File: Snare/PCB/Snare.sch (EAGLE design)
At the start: 91 parts, among them IC1 LM741P, IC10 LM741P, IC6 LM741P, IC7 LM741P, IC8 LM741P, IC9 LM741P, Q3 2N2222A, Q4 2N2222A, T1 2N3904, T5 2N3904, T6 2N3904

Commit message: Updated Snare schematic
updated snare schematic
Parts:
- added R11: 4.7k, resistor:R-US_0207/10
- added R12: 10k, rcl:R-TRIMM64W
- R1: value 10k -> 2k
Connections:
- removed net VCA_OUT: IC10.OUT, R60.1, R9.2
- new net DRUM_OUTPUT: C47.1, IC9.OUT, R12.E, R55.1, R56.2
- net AGND: now also R11.2, R12.A
- net N$27: now also R11.1
- net POT1A: now also R12.S; no longer C47.1, IC9.OUT, R55.1, R56.2
- net SW1: now also IC10.OUT, R60.1
- net SW2: now also R9.2
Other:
- note added: "Note: 1) POT1A is the drum output 2) The third pin of POT1 should be grounded 3) POT1B should be the middle pin of the POT"
- note added: "Note: 1) Switch turns the snare on/off 2) SW1 and SW2 normally connected 3) SW3 should be left open on the pot board"
- note removed: "Note: The third pin of POT1 should be grounded POT1B should be the middle pin"
- moved on the sheet: C38, R44

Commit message: Started PCB
Started working on the PCB
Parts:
- R100: value 2k -> 47k
- R101: value 2k -> 100k
- renumbered 100K to R101, 47K to R100
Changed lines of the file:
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@@
 <part name="IC6" library="linear" library_urn="urn:adsk.eagle:library:262" deviceset="*741" device="P" package3d_urn="urn:adsk.eagle:package:16409/2" technology="LM"/>
 <part name="C35" library="resistor" library_urn="urn:adsk.eagle:library:348" deviceset="C-EU" device="050-024X044" package3d_urn="urn:adsk.eagle:package:26162/1" value="0.1uF"/>
-<part name="100K" library="resistor" library_urn="urn:adsk.eagle:library:348" deviceset="R-US_" device="0207/10" package3d_urn="urn:adsk.eagle:package:25939/1" value="2k"/>
+<part name="R101" library="resistor" library_urn="urn:adsk.eagle:library:348" deviceset="R-US_" device="0207/10" package3d_urn="urn:adsk.eagle:package:25939/1" value="100k"/>
 <part name="C36" library="resistor" library_urn="urn:adsk.eagle:library:348" deviceset="C-EU" device="050-024X044" package3d_urn="urn:adsk.eagle:package:26162/1" value="0.1uF"/>
 <part name="C37" library="resistor" library_urn="urn:adsk.eagle:library:348" deviceset="C-EU" device="050-024X044" package3d_urn="urn:adsk.eagle:package:26162/1" value="0.1uF"/>
-<part name="47K" library="resistor" library_urn="urn:adsk.eagle:library:348" deviceset="R-US_" device="0207/10" package3d_urn="urn:adsk.eagle:package:25939/1" value="2k"/>
+<part name="R100" library="resistor" library_urn="urn:adsk.eagle:library:348" deviceset="R-US_" device="0207/10" package3d_urn="urn:adsk.eagle:package:25939/1" value="47k"/>
 <part name="IC7" library="linear" library_urn="urn:adsk.eagle:library:262" deviceset="*741" device="P" package3d_urn="urn:adsk.eagle:package:16409/2" technology="LM"/>
 <part name="C38" library="resistor" library_urn="urn:adsk.eagle:library:348" deviceset="C-EU" device="050-024X044" package3d_urn="urn:adsk.eagle:package:26162/1" value="1nF"/>
@@
 <attribute name="VALUE" x="38.481" y="257.556" size="1.778" layer="96" rot="R270"/>
 </instance>
-<instance part="100K" gate="G$1" x="88.9" y="287.02" smashed="yes" rot="R180">
+<instance part="R101" gate="G$1" x="88.9" y="287.02" smashed="yes" rot="R180">
 <attribute name="NAME" x="90.17" y="285.5214" size="1.778" layer="95" rot="R180"/>
 <attribute name="VALUE" x="92.71" y="290.322" size="1.778" layer="96" rot="R180"/>
@@
 <attribute name="VALUE" x="86.741" y="275.336" size="1.778" layer="96" rot="R270"/>
 </instance>
-<instance part="47K" gate="G$1" x="55.88" y="259.08" smashed="yes" rot="R180">
+<instance part="R100" gate="G$1" x="55.88" y="259.08" smashed="yes" rot="R180">
 <attribute name="NAME" x="57.15" y="257.5814" size="1.778" layer="95" rot="R180"/>
 <attribute name="VALUE" x="59.69" y="262.382" size="1.778" layer="96" rot="R180"/>
@@
 <pinref part="IC6" gate="A" pin="-IN"/>
 <wire x1="76.2" y1="259.08" x2="71.12" y2="259.08" width="0.1524" layer="91"/>
-<pinref part="100K" gate="G$1" pin="2"/>
+<pinref part="R101" gate="G$1" pin="2"/>
 <wire x1="71.12" y1="259.08" x2="71.12" y2="287.02" width="0.1524" layer="91"/>
 <wire x1="71.12" y1="287.02" x2="83.82" y2="287.02" width="0.1524" layer="91"/>
-<pinref part="47K" gate="G$1" pin="1"/>
+<pinref part="R100" gate="G$1" pin="1"/>
 <wire x1="71.12" y1="259.08" x2="60.96" y2="259.08" width="0.1524" layer="91"/>
 <junction x="71.12" y="259.08"/>
@@
 <net name="WHITE_NOISE_AMP" class="0">
 <segment>
-<pinref part="100K" gate="G$1" pin="1"/>
+<pinref part="R101" gate="G$1" pin="1"/>
 <wire x1="93.98" y1="287.02" x2="116.84" y2="287.02" width="0.1524" layer="91"/>
 <wire x1="116.84" y1="287.02" x2="116.84" y2="261.62" width="0.1524" layer="91"/>
@@
 <net name="N$28" class="0">
 <segment>
-<pinref part="47K" gate="G$1" pin="2"/>
+<pinref part="R100" gate="G$1" pin="2"/>
 <pinref part="C35" gate="G$1" pin="1"/>
 <wire x1="50.8" y1="259.08" x2="45.72" y2="259.08" width="0.1524" layer="91"/>

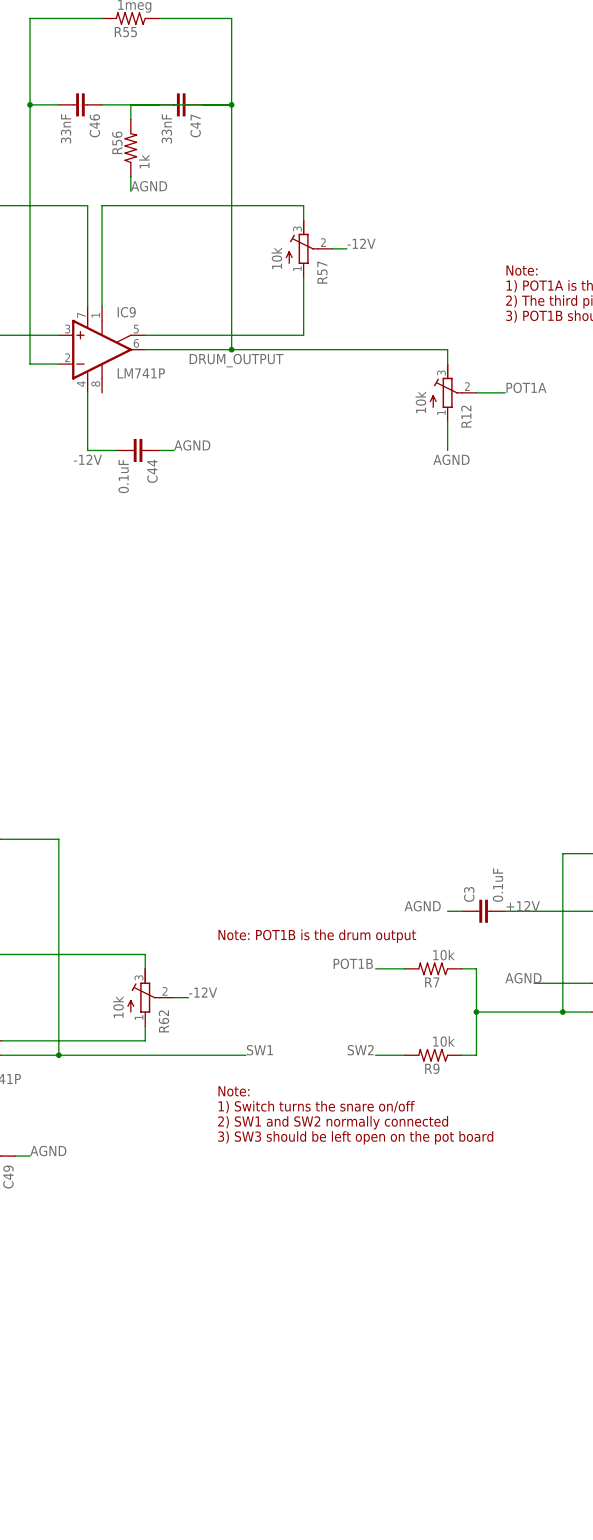
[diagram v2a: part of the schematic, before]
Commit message: Finished PCB
Finished the snare PCB
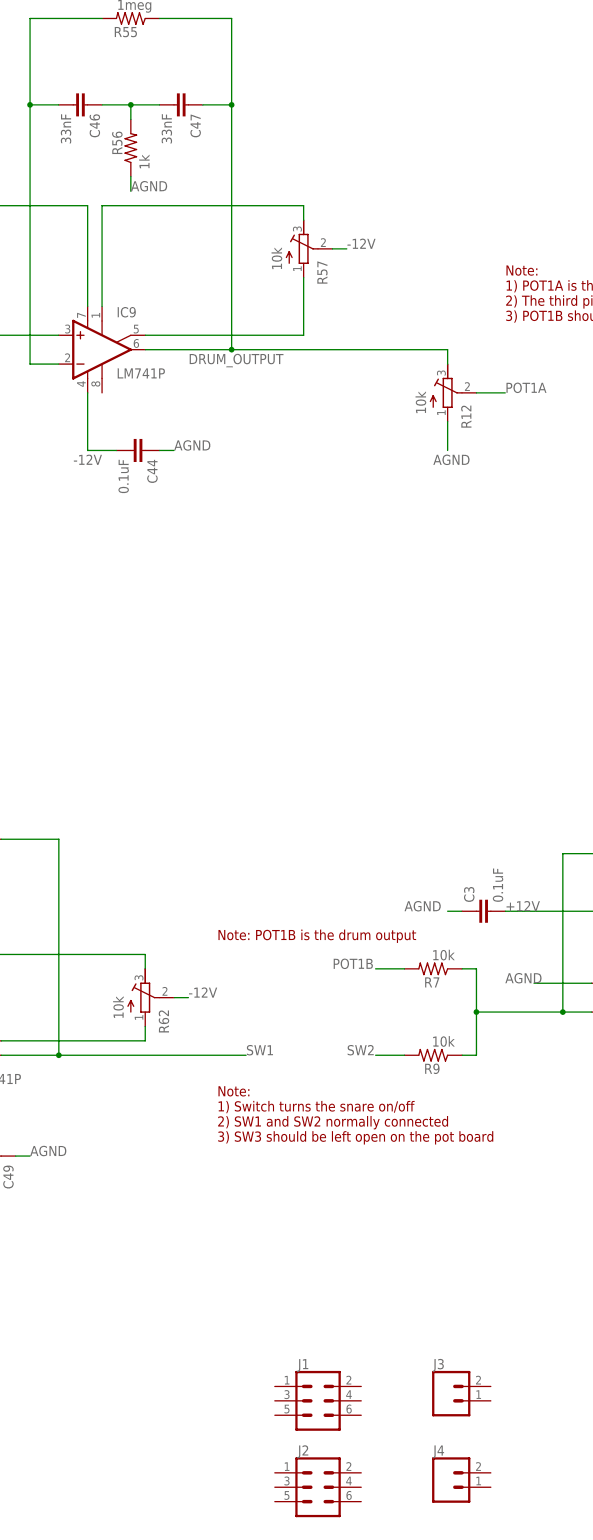
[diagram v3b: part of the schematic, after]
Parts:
- added J1, J2: (no value), SparkFun-Connectors:CONN_03X2NO_SILK
- added J3, J4: (no value), SparkFun-Connectors:CONN_021X02_NO_SILK
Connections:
- removed net N$44: C46.1, C47.2
- new net N$8: C46.1, C47.2, R56.2
- net DRUM_OUTPUT: no longer R56.2
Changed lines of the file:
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@@
 <part name="R11" library="resistor" library_urn="urn:adsk.eagle:library:348" deviceset="R-US_" device="0207/10" package3d_urn="urn:adsk.eagle:package:25939/1" value="4.7k"/>
 <part name="R12" library="rcl" library_urn="urn:adsk.eagle:library:334" deviceset="R-TRIMM" device="64W" package3d_urn="urn:adsk.eagle:package:23748/1" value="10k"/>
+<part name="J1" library="SparkFun-Connectors" deviceset="CONN_03X2" device="NO_SILK"/>
+<part name="J2" library="SparkFun-Connectors" deviceset="CONN_03X2" device="NO_SILK"/>
+<part name="J3" library="SparkFun-Connectors" deviceset="CONN_02" device="1X02_NO_SILK"/>
+<part name="J4" library="SparkFun-Connectors" deviceset="CONN_02" device="1X02_NO_SILK"/>
 </parts>
 <sheets>
@@
 <attribute name="NAME" x="377.571" y="250.19" size="1.778" layer="95" rot="R90"/>
 <attribute name="VALUE" x="369.57" y="252.73" size="1.778" layer="96" rot="R90"/>
+</instance>
+<instance part="J1" gate="G$1" x="350.52" y="78.74" smashed="yes">
+<attribute name="NAME" x="346.964" y="84.328" size="1.778" layer="95" font="vector"/>
+<attribute name="VALUE" x="347.218" y="72.898" size="1.778" layer="96" font="vector" align="top-left"/>
+</instance>
+<instance part="J2" gate="G$1" x="350.52" y="63.5" smashed="yes">
+<attribute name="NAME" x="346.964" y="69.088" size="1.778" layer="95" font="vector"/>
+<attribute name="VALUE" x="347.218" y="57.658" size="1.778" layer="96" font="vector" align="top-left"/>
+</instance>
+<instance part="J3" gate="G$1" x="373.38" y="78.74" smashed="yes">
+<attribute name="VALUE" x="370.84" y="73.914" size="1.778" layer="96" font="vector"/>
+<attribute name="NAME" x="370.84" y="84.328" size="1.778" layer="95" font="vector"/>
+</instance>
+<instance part="J4" gate="G$1" x="373.38" y="63.5" smashed="yes">
+<attribute name="VALUE" x="370.84" y="58.674" size="1.778" layer="96" font="vector"/>
+<attribute name="NAME" x="370.84" y="69.088" size="1.778" layer="95" font="vector"/>
 </instance>
 </instances>
@@
 </segment>
 </net>
-<net name="N$44" class="0">
-<segment>
-<pinref part="C46" gate="G$1" pin="1"/>
-<pinref part="C47" gate="G$1" pin="2"/>
-<wire x1="312.42" y1="307.34" x2="322.58" y2="307.34" width="0.1524" layer="91"/>
-</segment>
-</net>
 <net name="N$48" class="0">
 <segment>
@@
 <pinref part="R55" gate="G$1" pin="1"/>
 <wire x1="322.58" y1="322.58" x2="335.28" y2="322.58" width="0.1524" layer="91"/>
+<pinref part="IC9" gate="A" pin="OUT"/>
 <wire x1="335.28" y1="322.58" x2="335.28" y2="307.34" width="0.1524" layer="91"/>
-<pinref part="IC9" gate="A" pin="OUT"/>
 <wire x1="335.28" y1="307.34" x2="335.28" y2="264.16" width="0.1524" layer="91"/>
 <wire x1="335.28" y1="264.16" x2="320.04" y2="264.16" width="0.1524" layer="91"/>
 <label x="327.66" y="261.62" size="1.778" layer="95"/>
-<pinref part="C47" gate="G$1" pin="1"/>
-<wire x1="330.2" y1="307.34" x2="335.28" y2="307.34" width="0.1524" layer="91"/>
-<junction x="335.28" y="307.34"/>
-<pinref part="R56" gate="G$1" pin="2"/>
-<wire x1="335.28" y1="307.34" x2="317.5" y2="307.34" width="0.1524" layer="91"/>
-<wire x1="317.5" y1="307.34" x2="317.5" y2="304.8" width="0.1524" layer="91"/>
 <wire x1="335.28" y1="264.16" x2="373.38" y2="264.16" width="0.1524" layer="91"/>
 <junction x="335.28" y="264.16"/>
 <pinref part="R12" gate="G$1" pin="E"/>
 <wire x1="373.38" y1="261.62" x2="373.38" y2="264.16" width="0.1524" layer="91"/>
-</segment>
-</net>
+<pinref part="C47" gate="G$1" pin="1"/>
+<wire x1="330.2" y1="307.34" x2="335.28" y2="307.34" width="0.1524" layer="91"/>
+<junction x="335.28" y="307.34"/>
+</segment>
+</net>
+<net name="N$8" class="0">
+<segment>
+<pinref part="R56" gate="G$1" pin="2"/>
+<wire x1="317.5" y1="307.34" x2="317.5" y2="304.8" width="0.1524" layer="91"/>
+<pinref part="C46" gate="G$1" pin="1"/>
+<wire x1="312.42" y1="307.34" x2="317.5" y2="307.34" width="0.1524" layer="91"/>
+<pinref part="C47" gate="G$1" pin="2"/>
+<wire x1="317.5" y1="307.34" x2="322.58" y2="307.34" width="0.1524" layer="91"/>
+<junction x="317.5" y="307.34"/>
+</segment>
+</net>

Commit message: Finished Silkscreen
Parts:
- removed C38: 1nF, resistor:C-EU050-024X044
- removed C41: 2.2u, resistor:C-EU050-024X044
- removed C42: 10uF, rcl:CPOL-USE2.5-6
- removed C43, C44, C45, C49, C50: 0.1uF, resistor:C-EU050-024X044
- removed C47: 33nF, resistor:C-EU050-024X044
- removed D6: 200mA/100V/1V, SparkFun-DiscreteSemi:DIODE-1N4148
- removed R100, R51: 47k, resistor:R-US_0207/10
- removed R101: 100k, resistor:R-US_0207/10
- removed R34: 680k, resistor:R-US_0207/10
- removed R39, R40: 2k, resistor:R-US_0207/10
- removed R46: 15k, resistor:R-US_0207/10
- removed R49: 10k, resistor:R-US_0207/10
- removed R50: 220, resistor:R-US_0207/10
- added C10, C6, C9: 0.1uF, resistor:C-EU050-024X044
- added C13, C14, C16: 10uF, rcl:CPOL-USE2.5-6
- added C17, C18: 1u, resistor:C-EU050-024X044
- added C4: 1nF, resistor:C-EU050-024X044
- added D2: 200mA/100V/1V, SparkFun-DiscreteSemi:DIODE-1N4148
- added R13: 1k, resistor:R-US_0207/10
- added R14, R16: 100k, resistor:R-US_0207/10
- added R15, R17, R18: 10k, resistor:R-US_0207/10
- added TRIM3, TRIM4, TRIM6: 10k, rcl:R-TRIMM64W
- C15: value 0.33uF -> 10uF; device resistor:C-EU050-024X044 -> rcl:CPOL-USE2.5-6
- C2: value 0.1uF -> 1nF
- C20: value 1nF -> 0.33uF
- C23: value 2.2u -> 0.1uF
- C24, C28: value 10uF -> 0.1uF; device rcl:CPOL-USE2.5-6 -> resistor:C-EU050-024X044
- C26, C29: value 1u -> 0.1uF
- C27: value 1u -> 33nF
- C3: value 0.1uF -> 10uF; device resistor:C-EU050-024X044 -> rcl:CPOL-USE2.5-6
- C30: value 0.1uF -> 2.2u
- C31: value 10uF -> 1u; device rcl:CPOL-USE2.5-6 -> resistor:C-EU050-024X044
- C32: value 10uF -> 2.2u; device rcl:CPOL-USE2.5-6 -> resistor:C-EU050-024X044
- R1: value 2k -> 15k
- R10: device rcl:R-TRIMM64W -> resistor:R-US_0207/10
- R11: value 4.7k -> 2k
- R12: value 10k -> 4.7k; device rcl:R-TRIMM64W -> resistor:R-US_0207/10
- R2: value 100k -> 47k
- R3, R4: value 10k -> 2k
- R35: value 1k -> 10k
- R36: value 100k -> 10k
- R38: value 4.7k -> 1k
- R43: value 2k -> 220
- R44: value 15k -> 10k
- R45: value 10k -> 47k
- R5: value 10k -> 15k
- R6: value 1k -> 2k
- R7: value 10k -> 4.7k
- R8: value 10k -> 680k; device rcl:R-TRIMM64W -> resistor:R-US_0207/10
- R9: value 10k -> 100k
- renumbered C34 to C5, C35 to C1, C36 to C8, C37 to C7, C39 to C12, C40 to C11, C46 to C25, C48 to C19, IC10 to IC4, IC7 to IC3, IC8 to IC2, IC9 to IC5, R47 to R41, R48 to R42, R52 to R20, R53 to R27, R54 to R29, R55 to R31, R56 to R32, R57 to TRIM5, R58 to R21, R59 to R28, R60 to R30, R61 to R22, R62 to TRIM2, R63 to TRIM1, R64 to R23, R65 to R19, R66 to R25, R67 to R26, T1 to Q1, T5 to Q2, T6 to Q6, U$1 to Q5
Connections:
- net +12V: now also C15.+, C17.2, C21.2, C23.1, C28.2, C9.2, R3.1, R43.2; no longer C22.2, C24.+, C27.2, C3.2, C45.1, C50.2, R39.1, R50.2
- net -12V: now also C10.2, C16.-, C18.1, C24.2, C26.2, C29.2, R4.2, R44.1, TRIM4.S; no longer C2.2, C21.2, C28.-, C29.1, C44.2, C49.2, R10.S, R40.2, R49.1
- net AGND: now also C10.1, C15.-, C16.+, C17.1, C18.2, C20.1, C23.2, C24.1, C26.1, C28.1, C29.1, C31.2, C33.-, C4.2, C9.1, R14.2, R45.1, R5.2, R6.2, R7.2, TRIM6.A; no longer C15.1, C2.1, C20.2, C22.1, C24.-, C26.2, C27.1, C28.+, C29.2, C3.1, C42.-, C44.1, C45.2, C49.1, C50.1, R1.2, R11.2, R12.A, R2.2, R44.2, R51.1
- net CC_INPUT: now also C30.2, IC6.OUT, TRIM3.S; no longer C23.2, IC1.OUT, R8.S
- net DRUM_OUTPUT: now also C27.1, TRIM6.E; no longer C47.1, R12.E
- net LOW_FREQ_WN: now also R10.1, R15.2; no longer R3.2, R45.1
- net N$1: now also R15.1, R17.1, R18.2; no longer R3.1, R4.2, R5.1
- net N$2: now also IC6.-IN, R35.1, R36.1, R38.2; no longer IC1.-IN, R6.2, R7.1, R9.1
- net N$20: now also C6.1, R8.2; no longer C30.1, R34.2
- net N$21: now also C14.-, C3.-, R13.2, R16.2, R4.1; no longer C31.-, C33.-, R35.2, R36.2, R40.1
- net N$23: now also IC1.-IN, R2.1, R9.2; no longer IC6.-IN, R100.1, R101.2
- net N$27: now also R11.2, R7.1; no longer R11.1, R43.2
- net N$28: now also R2.2; no longer R100.2
- net N$3: now also R38.1, TRIM3.A; no longer R6.1, R8.A
- net N$30: now also C13.+, R12.2; no longer C32.+, R38.2
- net N$32: now also C2.1, R5.1; no longer C38.1, R44.1
- net N$33: now also R10.2, R6.1; no longer R1.1, R45.2
- net N$34: now also C4.1, R1.2; no longer C20.1, R46.2
- net N$36: now also C20.2, C22.2, D2.C; no longer C15.2, C43.2, D1.C
- net N$37: now also C30.1; no longer C23.1
- net N$38: now also C32.1, R44.2; no longer C41.1, R49.2
- net N$39: now also C31.1, C33.+, R43.1; no longer C26.1, C42.+, R50.1
- net N$4: now also IC6.ON2, TRIM4.A; no longer IC1.ON2, R10.A
- net N$40: now also D2.A, Q4.E; no longer D1.A, Q3.E
- net N$41: now also C22.1; no longer C43.1
- net N$5: now also C14.+, R13.1; no longer C31.+, R35.1
- net N$51: now also D1.C; no longer D6.C
- net N$53: now also D1.A, Q3.E; no longer D6.A, Q4.E
- net N$6: now also C3.+, C6.2, R12.1, R3.2, R8.1; no longer C30.2, C33.+, R34.1, R38.1, R39.2
- net N$7: now also IC6.ON1, TRIM4.E; no longer IC1.ON1, R10.E
- net N$8: now also C27.2; no longer C47.2
- net OUTPUT: now also C32.2, R45.2; no longer C41.2, R51.2
- net POT1A: now also TRIM6.S; no longer R12.S
- net POT1B: now also R35.2; no longer R7.2
- net POT2A: now also R11.1; no longer R43.1
- net POT2B: now also R17.2; no longer R5.2
- net SW2: now also R36.2; no longer R9.2
- net VCA_INPUT: now also R18.1; no longer R4.1
- net WHITE_NOISE: now also C13.-, R16.1; no longer C32.-, R36.1
- net WHITE_NOISE_AMP: now also C2.2, IC1.OUT, R1.1, R14.1, R9.1; no longer C38.2, IC6.OUT, R101.1, R2.1, R46.1
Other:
- note added: "Drum Hit"
- note added: "Extra Pins (In case I screwed something up)"
- note added: "Summing Amp and Common Collector"
- note added: "Voltage-Controlled Amplifier"
- note added: "WN High Pass Filter"
- note added: "WN Low Pass Filter"
- note added: "White Noise Amplifier"
- note added: "White Noise Generator"
- moved on the sheet: C2, C20, C21, C22, C23, C26, C27, C29, C30, C33, D1, IC1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
